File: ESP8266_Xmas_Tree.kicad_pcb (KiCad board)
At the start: 2 copper layers, 174.3 x 184.8 mm, 16 parts, among them U1 WeMos_D1_mini

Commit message: adding some nice graphics like gingerbreak man and snowflakes to silkscreen
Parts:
- added G***: LOGO, LOGO, F.Cu at (223.4, 166.2)
- added G***: LOGO, LOGO, F.Cu at (182.3, 139.6)
- added G***: LOGO, LOGO, F.Cu at (174.9, 199.7)
- added G***: LOGO, LOGO, F.Cu at (239.3, 147.6)
- added G***: LOGO, LOGO, F.Cu at (286.7, 199.3)
- added G***: LOGO, LOGO, F.Cu at (207.2, 91.3)
- added G***: LOGO, LOGO, F.Cu at (171.2, 164.9)
- added G***: LOGO, LOGO, F.Cu at (196.5, 110.1)
- added G***: LOGO, LOGO, F.Cu at (136.3, 199.6)
- added G***: LOGO, LOGO, F.Cu at (192.2, 191.7)
- added G***: LOGO, LOGO, F.Cu at (246.2, 196.8)
- added G***: LOGO, LOGO, F.Cu at (228.7, 120.6)
- added G***: LOGO, LOGO, F.Cu at (223.6, 213.9)
- added G***: LOGO, LOGO, F.Cu at (156.6, 186.7)
- added G***: LOGO, LOGO, F.Cu at (251.6, 167.6)
- moved D5 2.25 mm to (244.9, 160.5)
- moved D15 1.68 mm to (210.1, 67.6)

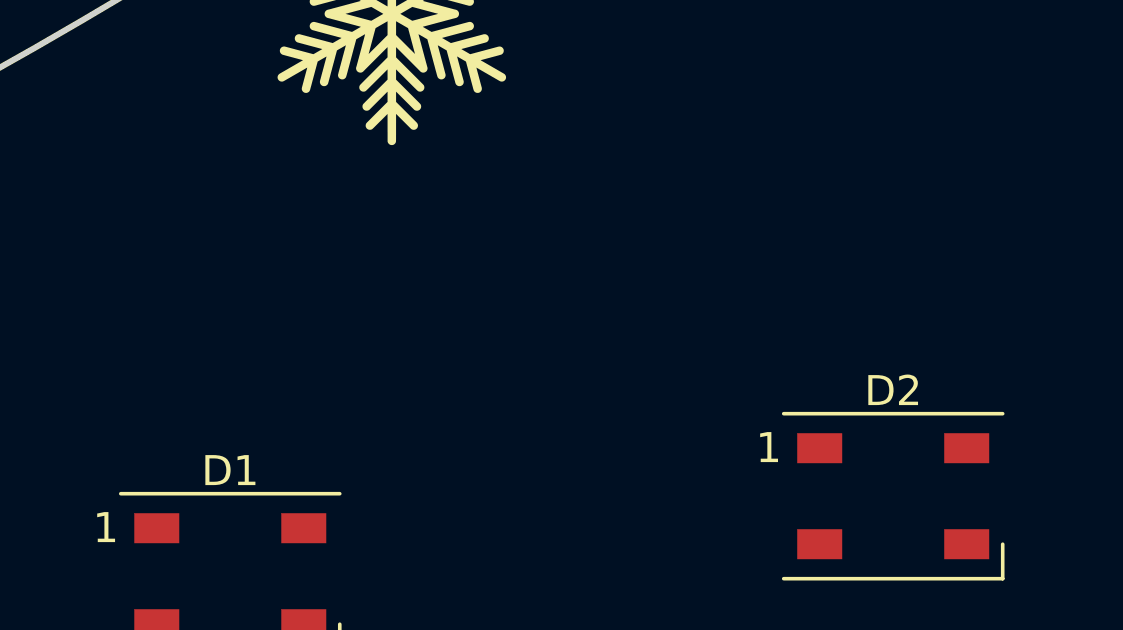
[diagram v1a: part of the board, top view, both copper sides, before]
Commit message: adding d1 mini step model to pcb
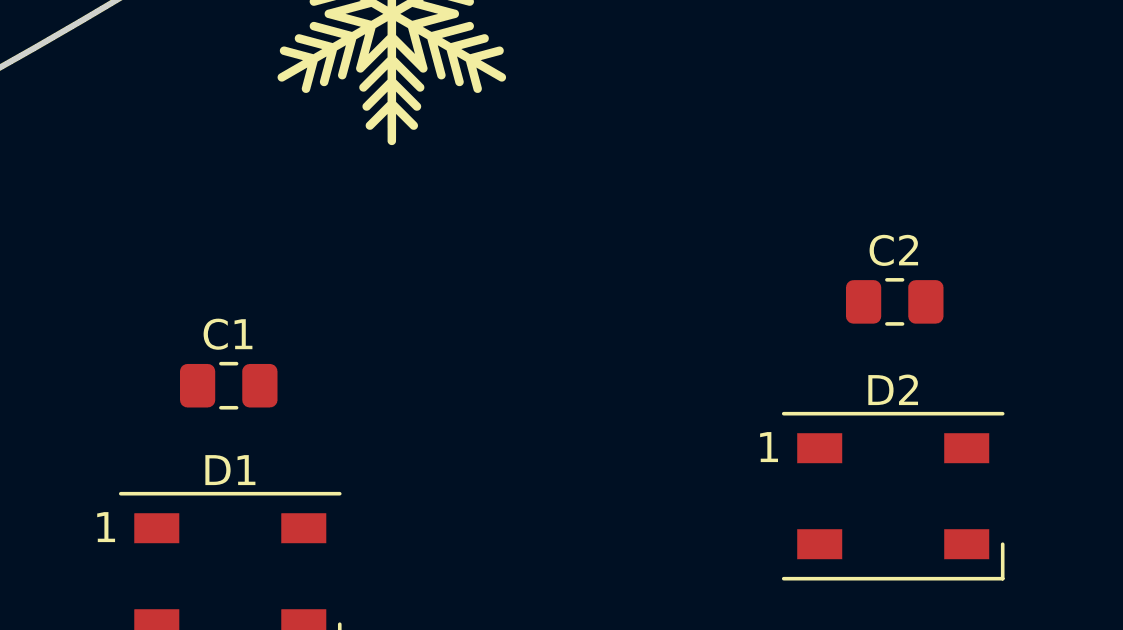
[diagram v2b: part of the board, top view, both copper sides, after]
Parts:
- added C1: C, Capacitor_SMD:C_0805_2012Metric_Pad1.18x1.45mm_HandSolder, F.Cu at (165.8, 177.3)
- added C2: C, Capacitor_SMD:C_0805_2012Metric_Pad1.18x1.45mm_HandSolder, F.Cu at (188.0, 174.5)
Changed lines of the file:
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@@
   (net 75 "unconnected-(U1-Pad15)")
   (net 76 "unconnected-(U1-Pad16)")
+  (net 77 "unconnected-(C1-Pad1)")
+  (net 78 "unconnected-(C1-Pad2)")
+  (net 79 "unconnected-(C2-Pad1)")
+  (net 80 "unconnected-(C2-Pad2)")
   (footprint "LOGO" (layer "F.Cu")
     (at 223.4184 166.2176)
@@
     )
   )
+  (footprint "Capacitor_SMD:C_0805_2012Metric_Pad1.18x1.45mm_HandSolder" (layer "F.Cu")
+    (at 188.0108 174.498)
+    (descr "Capacitor SMD 0805 (2012 Metric), square (rectangular) end terminal, IPC_7351 nominal with elongated pad for handsoldering. (Body size source: IPC-SM-782 page 76, https://www.pcb-3d.com/wordpress/wp-content/uploads/ipc-sm-782a_amendment_1_and_2.pdf, https://docs.google.com/spreadsheets/d/1BsfQQcO9C6DZCsRaXUlFlo91Tg2WpOkGARC1WS5S8t0/edit?usp=sharing), generated with kicad-footprint-generator")
+    (tags "capacitor handsolder")
+    (property "Sheetfile" "ESP8266_Xmas_Tree.kicad_sch")
+    (property "Sheetname" "")
+    (attr smd)
+    (fp_text reference "C2" (at 0 -1.68) (layer "F.SilkS")
+      (effects (font (size 1 1) (thickness 0.15)))
+    )
+    (fp_text value "C" (at 0 1.68) (layer "F.Fab")
+      (effects (font (size 1 1) (thickness 0.15)))
+    )
+    (fp_text user "${REFERENCE}" (at 0 0) (layer "F.Fab")
+      (effects (font (size 0.5 0.5) (thickness 0.08)))
+    )
+    (fp_line (start -0.261252 0.735) (end 0.261252 0.735) (layer "F.SilkS") (width 0.12))
+    (fp_line (start -0.261252 -0.735) (end 0.261252 -0.735) (layer "F.SilkS") (width 0.12))
+    (fp_line (start 1.88 0.98) (end -1.88 0.98) (layer "F.CrtYd") (width 0.05))
+    (fp_line (start 1.88 -0.98) (end 1.88 0.98) (layer "F.CrtYd") (width 0.05))
+    (fp_line (start -1.88 -0.98) (end 1.88 -0.98) (layer "F.CrtYd") (width 0.05))
+    (fp_line (start -1.88 0.98) (end -1.88 -0.98) (layer "F.CrtYd") (width 0.05))
+    (fp_line (start -1 -0.625) (end 1 -0.625) (layer "F.Fab") (width 0.1))
+    (fp_line (start 1 -0.625) (end 1 0.625) (layer "F.Fab") (width 0.1))
+    (fp_line (start -1 0.625) (end -1 -0.625) (layer "F.Fab") (width 0.1))
+    (fp_line (start 1 0.625) (end -1 0.625) (layer "F.Fab") (width 0.1))
+    (pad "1" smd roundrect (at -1.0375 0) (size 1.175 1.45) (layers "F.Cu" "F.Paste" "F.Mask") (roundrect_rratio 0.212766)
+      (net 79 "unconnected-(C2-Pad1)") (pintype "passive"))
+    (pad "2" smd roundrect (at 1.0375 0) (size 1.175 1.45) (layers "F.Cu" "F.Paste" "F.Mask") (roundrect_rratio 0.212766)
+      (net 80 "unconnected-(C2-Pad2)") (pintype "passive"))
+    (model "${KICAD6_3DMODEL_DIR}/Capacitor_SMD.3dshapes/C_0805_2012Metric.wrl"
+      (offset (xyz 0 0 0))
+      (scale (xyz 1 1 1))
+      (rotate (xyz 0 0 0))
+    )
+  )
   (footprint "LED_SMD:LED_WS2812B_PLCC4_5.0x5.0mm_P3.2mm" (layer "F.Cu")
     (at 201.295 123.825)
@@
     )
   )
+  (footprint "Capacitor_SMD:C_0805_2012Metric_Pad1.18x1.45mm_HandSolder" (layer "F.Cu")
+    (at 165.8112 177.292)
+    (descr "Capacitor SMD 0805 (2012 Metric), square (rectangular) end terminal, IPC_7351 nominal with elongated pad for handsoldering. (Body size source: IPC-SM-782 page 76, https://www.pcb-3d.com/wordpress/wp-content/uploads/ipc-sm-782a_amendment_1_and_2.pdf, https://docs.google.com/spreadsheets/d/1BsfQQcO9C6DZCsRaXUlFlo91Tg2WpOkGARC1WS5S8t0/edit?usp=sharing), generated with kicad-footprint-generator")
+    (tags "capacitor handsolder")
+    (property "Sheetfile" "ESP8266_Xmas_Tree.kicad_sch")
+    (property "Sheetname" "")
+    (attr smd)
+    (fp_text reference "C1" (at 0 -1.68) (layer "F.SilkS")
+      (effects (font (size 1 1) (thickness 0.15)))
+    )
+    (fp_text value "C" (at 0 1.68) (layer "F.Fab")
+      (effects (font (size 1 1) (thickness 0.15)))
+    )
+    (fp_text user "${REFERENCE}" (at 0 0) (layer "F.Fab")
+      (effects (font (size 0.5 0.5) (thickness 0.08)))
+    )
+    (fp_line (start -0.261252 -0.735) (end 0.261252 -0.735) (layer "F.SilkS") (width 0.12))
+    (fp_line (start -0.261252 0.735) (end 0.261252 0.735) (layer "F.SilkS") (width 0.12))
+    (fp_line (start 1.88 -0.98) (end 1.88 0.98) (layer "F.CrtYd") (width 0.05))
+    (fp_line (start -1.88 -0.98) (end 1.88 -0.98) (layer "F.CrtYd") (width 0.05))
+    (fp_line (start 1.88 0.98) (end -1.88 0.98) (layer "F.CrtYd") (width 0.05))
+    (fp_line (start -1.88 0.98) (end -1.88 -0.98) (layer "F.CrtYd") (width 0.05))
+    (fp_line (start -1 -0.625) (end 1 -0.625) (layer "F.Fab") (width 0.1))
+    (fp_line (start 1 0.625) (end -1 0.625) (layer "F.Fab") (width 0.1))
+    (fp_line (start 1 -0.625) (end 1 0.625) (layer "F.Fab") (width 0.1))
+    (fp_line (start -1 0.625) (end -1 -0.625) (layer "F.Fab") (width 0.1))
+    (pad "1" smd roundrect (at -1.0375 0) (size 1.175 1.45) (layers "F.Cu" "F.Paste" "F.Mask") (roundrect_rratio 0.212766)
+      (net 77 "unconnected-(C1-Pad1)") (pintype "passive"))
+    (pad "2" smd roundrect (at 1.0375 0) (size 1.175 1.45) (layers "F.Cu" "F.Paste" "F.Mask") (roundrect_rratio 0.212766)
+      (net 78 "unconnected-(C1-Pad2)") (pintype "passive"))
+    (model "${KICAD6_3DMODEL_DIR}/Capacitor_SMD.3dshapes/C_0805_2012Metric.wrl"
+      (offset (xyz 0 0 0))
+      (scale (xyz 1 1 1))
+      (rotate (xyz 0 0 0))
+    )
+  )
   (footprint "Module:WEMOS_D1_mini_light" (layer "B.Cu")
     (at 220.495 184.785 180)
@@
       (rotate (xyz 0 0 0))
     )
-    (model "${KICAD6_3DMODEL_DIR}/Connector_PinHeader_2.54mm.3dshapes/PinHeader_1x08_P2.54mm_Vertical.wrl"
+    (model "${KICAD6_3DMODEL_DIR}/Connector_PinHeader_2.54mm.3dshapes/PinHeader_1x08_P2.54mm_Vertical.wrl" hide
       (offset (xyz 0 0 9.5))
       (scale (xyz 1 1 1))
       (rotate (xyz 0 -180 0))
     )
-    (model "${KICAD6_3DMODEL_DIR}/Connector_PinHeader_2.54mm.3dshapes/PinHeader_1x08_P2.54mm_Vertical.wrl"
+    (model "${KICAD6_3DMODEL_DIR}/Connector_PinHeader_2.54mm.3dshapes/PinHeader_1x08_P2.54mm_Vertical.wrl" hide
       (offset (xyz 22.86 0 9.5))
       (scale (xyz 1 1 1))
@@
       (rotate (xyz 0 0 0))
     )
+    (model "${KIPRJMOD}/3D_Models/WEMOS-D1-mini.step"
+      (offset (xyz 24.25 -26.75 9.75))
+      (scale (xyz 1 1 1))
+      (rotate (xyz -90 0 0))
+    )
   )

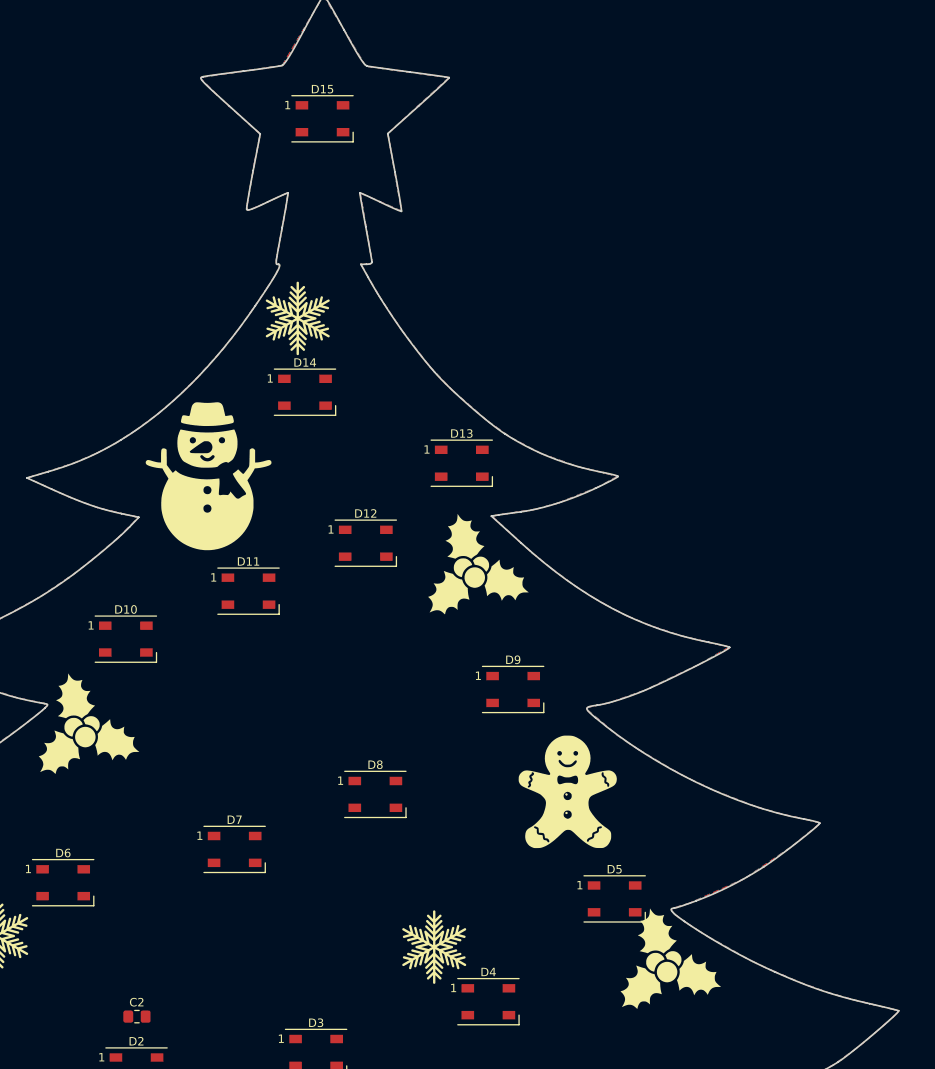
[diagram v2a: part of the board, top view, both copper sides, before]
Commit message: adding caps for WS2812B LEDs
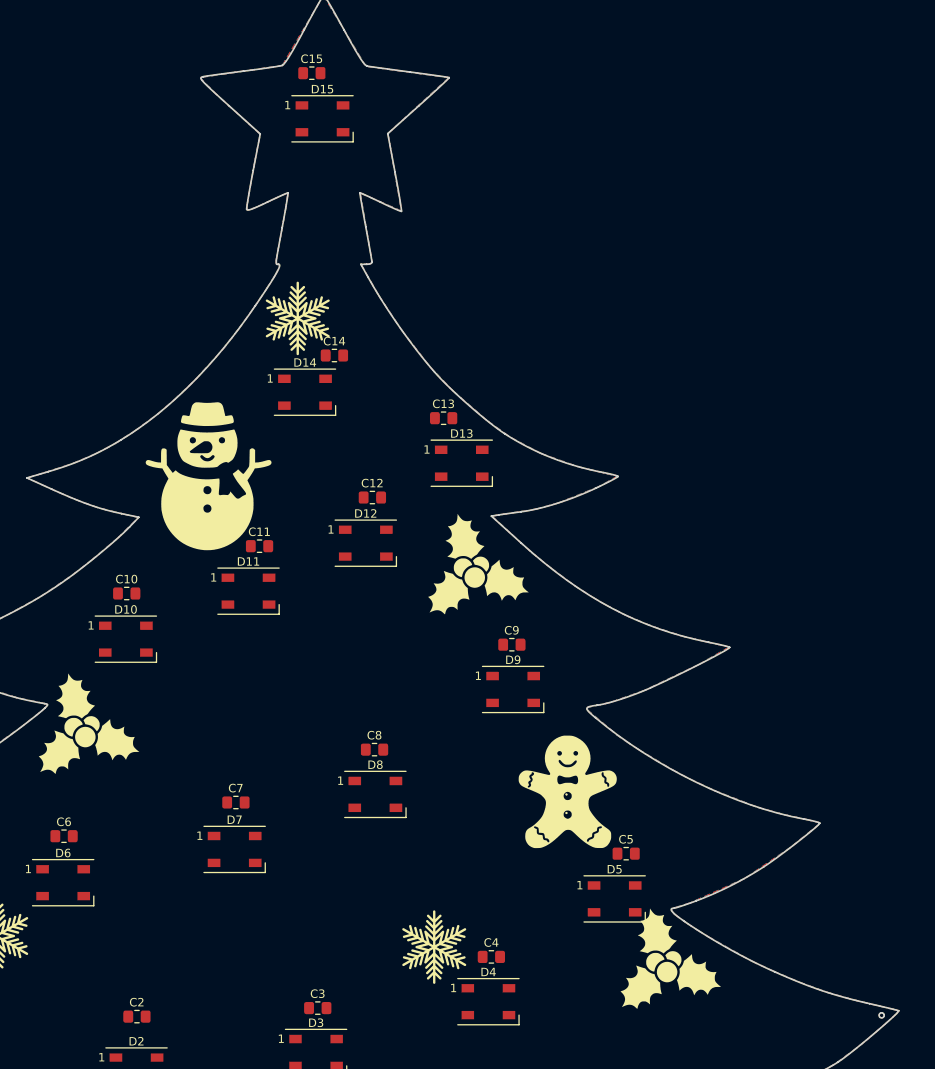
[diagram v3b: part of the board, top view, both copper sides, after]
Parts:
- added C10: C, Capacitor_SMD:C_0805_2012Metric_Pad1.18x1.45mm_HandSolder, F.Cu at (186.8, 124.1)
- added C11: C, Capacitor_SMD:C_0805_2012Metric_Pad1.18x1.45mm_HandSolder, F.Cu at (202.6, 118.5)
- added C12: C, Capacitor_SMD:C_0805_2012Metric_Pad1.18x1.45mm_HandSolder, F.Cu at (216.1, 112.7)
- added C13: C, Capacitor_SMD:C_0805_2012Metric_Pad1.18x1.45mm_HandSolder, F.Cu at (224.5, 103.2)
- added C14: C, Capacitor_SMD:C_0805_2012Metric_Pad1.18x1.45mm_HandSolder, F.Cu at (211.5, 95.8)
- added C15: C, Capacitor_SMD:C_0805_2012Metric_Pad1.18x1.45mm_HandSolder, F.Cu at (208.8, 62.1)
- added C3: C, Capacitor_SMD:C_0805_2012Metric_Pad1.18x1.45mm_HandSolder, F.Cu at (209.6, 173.5)
- added C4: C, Capacitor_SMD:C_0805_2012Metric_Pad1.18x1.45mm_HandSolder, F.Cu at (230.2, 167.4)
- added C5: C, Capacitor_SMD:C_0805_2012Metric_Pad1.18x1.45mm_HandSolder, F.Cu at (246.3, 155.1)
- added C6: C, Capacitor_SMD:C_0805_2012Metric_Pad1.18x1.45mm_HandSolder, F.Cu at (179.3, 153.0)
- added C7: C, Capacitor_SMD:C_0805_2012Metric_Pad1.18x1.45mm_HandSolder, F.Cu at (199.8, 149.0)
- added C8: C, Capacitor_SMD:C_0805_2012Metric_Pad1.18x1.45mm_HandSolder, F.Cu at (216.3, 142.7)
- added C9: C, Capacitor_SMD:C_0805_2012Metric_Pad1.18x1.45mm_HandSolder, F.Cu at (232.7, 130.2)
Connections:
- C1 pad 1: unconnected-(C1-Pad1) -> +3.3V
- C1 pad 2: unconnected-(C1-Pad2) -> GND
- C2 pad 1: unconnected-(C2-Pad1) -> +3.3V
- C2 pad 2: unconnected-(C2-Pad2) -> GND
- D1 pad 1: unconnected-(D1-Pad1) -> +3.3V
- D1 pad 2: unconnected-(D1-Pad2) -> Net-(D1-Pad2)
- D1 pad 3: unconnected-(D1-Pad3) -> GND
- D10 pad 1: unconnected-(D10-Pad1) -> +3.3V
- D10 pad 2: unconnected-(D10-Pad2) -> Net-(D13-Pad4)
- D10 pad 3: unconnected-(D10-Pad3) -> GND
- D10 pad 4: unconnected-(D10-Pad4) -> Net-(D10-Pad4)
- D11 pad 1: unconnected-(D11-Pad1) -> +3.3V
- D11 pad 2: unconnected-(D11-Pad2) -> Net-(D11-Pad2)
- D11 pad 3: unconnected-(D11-Pad3) -> GND
- D11 pad 4: unconnected-(D11-Pad4) -> Net-(D8-Pad2)
- D12 pad 1: unconnected-(D12-Pad1) -> +3.3V
- D12 pad 2: unconnected-(D12-Pad2) -> Net-(D12-Pad2)
- D12 pad 3: unconnected-(D12-Pad3) -> GND
- D12 pad 4: unconnected-(D12-Pad4) -> Net-(D9-Pad2)
- D13 pad 1: unconnected-(D13-Pad1) -> +3.3V
- D13 pad 3: unconnected-(D13-Pad3) -> GND
- D13 pad 4: unconnected-(D13-Pad4) -> Net-(D13-Pad4)
- D14 pad 1: unconnected-(D14-Pad1) -> +3.3V
- D14 pad 3: unconnected-(D14-Pad3) -> GND
- D14 pad 4: unconnected-(D14-Pad4) -> Net-(D11-Pad2)
- D15 pad 1: unconnected-(D15-Pad1) -> +3.3V
- D15 pad 3: unconnected-(D15-Pad3) -> GND
- D15 pad 4: unconnected-(D15-Pad4) -> Net-(D12-Pad2)
- D2 pad 1: unconnected-(D2-Pad1) -> +3.3V
- D2 pad 2: unconnected-(D2-Pad2) -> Net-(D5-Pad4)
- D2 pad 3: unconnected-(D2-Pad3) -> GND
- D3 pad 1: unconnected-(D3-Pad1) -> +3.3V
- D3 pad 2: unconnected-(D3-Pad2) -> Net-(D6-Pad4)
- D3 pad 3: unconnected-(D3-Pad3) -> GND
- D4 pad 1: unconnected-(D4-Pad1) -> +3.3V
- D4 pad 2: unconnected-(D4-Pad2) -> Net-(D4-Pad2)
- D4 pad 3: unconnected-(D4-Pad3) -> GND
- D4 pad 4: unconnected-(D4-Pad4) -> Net-(D1-Pad2)
- D5 pad 1: unconnected-(D5-Pad1) -> +3.3V
- D5 pad 2: unconnected-(D5-Pad2) -> Net-(D8-Pad4)
- D5 pad 3: unconnected-(D5-Pad3) -> GND
- D5 pad 4: unconnected-(D5-Pad4) -> Net-(D5-Pad4)
- D6 pad 1: unconnected-(D6-Pad1) -> +3.3V
- D6 pad 2: unconnected-(D6-Pad2) -> Net-(D9-Pad4)
- D6 pad 3: unconnected-(D6-Pad3) -> GND
- D6 pad 4: unconnected-(D6-Pad4) -> Net-(D6-Pad4)
- D7 pad 1: unconnected-(D7-Pad1) -> +3.3V
- D7 pad 2: unconnected-(D7-Pad2) -> Net-(D10-Pad4)
- D7 pad 3: unconnected-(D7-Pad3) -> GND
- D7 pad 4: unconnected-(D7-Pad4) -> Net-(D4-Pad2)
- D8 pad 1: unconnected-(D8-Pad1) -> +3.3V
- D8 pad 2: unconnected-(D8-Pad2) -> Net-(D8-Pad2)
- D8 pad 3: unconnected-(D8-Pad3) -> GND
- D8 pad 4: unconnected-(D8-Pad4) -> Net-(D8-Pad4)
- D9 pad 1: unconnected-(D9-Pad1) -> +3.3V
- D9 pad 2: unconnected-(D9-Pad2) -> Net-(D9-Pad2)
- D9 pad 3: unconnected-(D9-Pad3) -> GND
- D9 pad 4: unconnected-(D9-Pad4) -> Net-(D9-Pad4)
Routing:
- net GND: vias 0 -> 1
- added copper zone on B.Cu, net GND
- added copper zone on F.Cu, net GND
- removed copper zone on B.Cu, net (none)
- removed copper zone on F.Cu, net (none)

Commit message: adding 3V3 and GND to MCU
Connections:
- D13 pad 2: unconnected-(D13-Pad2) -> Net-(D2-Pad4)
- D14 pad 2: unconnected-(D14-Pad2) -> Net-(D3-Pad4)
- D2 pad 4: unconnected-(D2-Pad4) -> Net-(D2-Pad4)
- D3 pad 4: unconnected-(D3-Pad4) -> Net-(D3-Pad4)
- U1 pad 10: unconnected-(U1-Pad10) -> GND
- U1 pad 8: unconnected-(U1-Pad8) -> +3.3V
- U1 pad 9: unconnected-(U1-Pad9) -> +5V

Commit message: adding Edge Cuts, Silkscreen an filled zones from SVG files
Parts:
- removed the G*** at (136.3, 199.6)
- removed the G*** at (251.6, 167.6)
- moved G*** 69.6 mm to (240.3, 173.4)
- moved G*** 67.9 mm to (168.1, 171.8)
- moved G*** 61.7 mm to (187.2, 130.1)
- moved G*** 21.8 mm to (264.9, 199.1)
- moved G*** 21.5 mm to (203.1, 207.4)
- moved C13 20.3 mm to (205.1, 97.2)
- moved D13 19.7 mm to (207.9, 102.7)
- moved C14 17.0 mm to (195.3, 100.8)
- moved D14 17.0 mm to (191.8, 105.2)
- moved G*** 16.6 mm to (144.0, 197.5)
- moved D6 16.2 mm to (164.5, 151.9)
- moved G*** 16.0 mm to (223.7, 144.3)
- moved G*** 14.9 mm to (160.0, 200.5)
- moved D1 13.8 mm to (154.1, 176.4)
- moved G*** 13.4 mm to (215.4, 119.0)
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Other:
- board size 174.3 x 184.8 mm -> 158.7 x 185.8 mm
